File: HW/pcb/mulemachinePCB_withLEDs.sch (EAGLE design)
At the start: 31 parts, among them IC1 LD117AV50, IC2 MEGA8-P, J1 DCJ0202, Q1 16Mhz

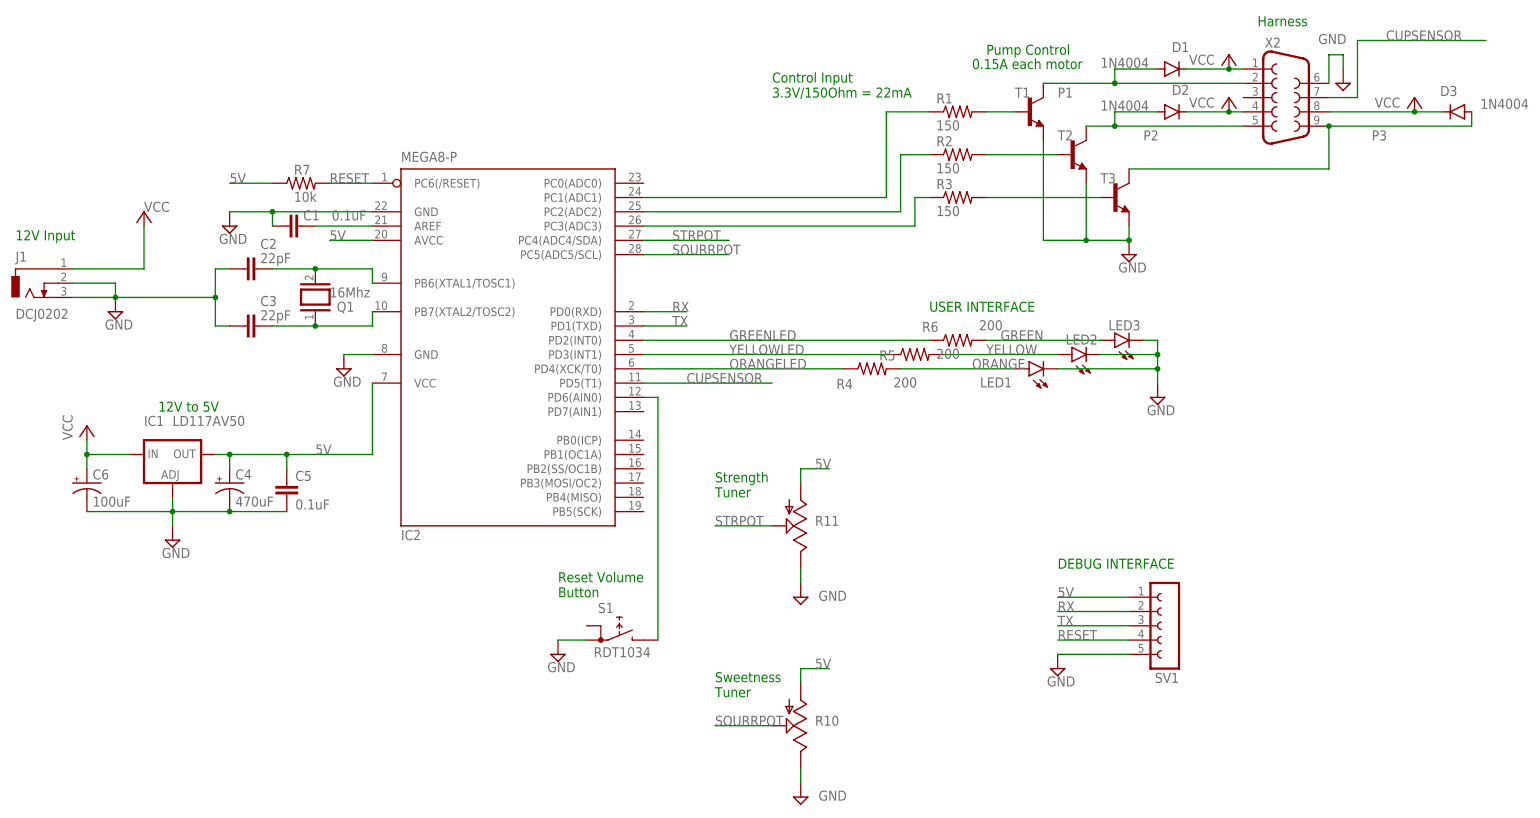
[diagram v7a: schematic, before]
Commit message: sourced push button and added to schematic and PCB layout. matched needed mounting to laser front panel cutout.
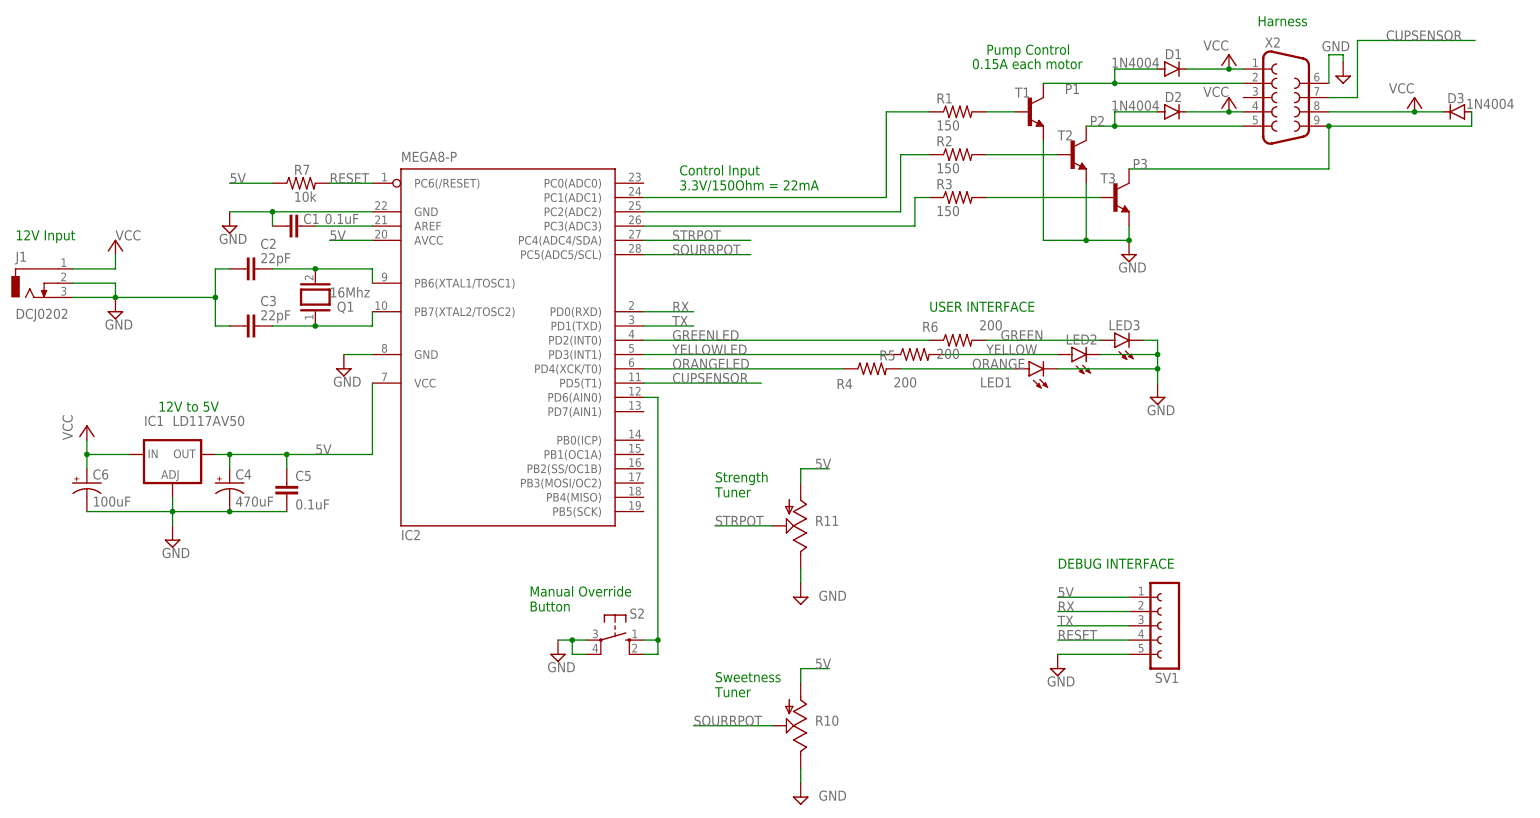
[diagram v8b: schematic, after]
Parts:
- removed S1: RDT1034, switch:RDT1034
- added S2: (no value), switch-omron:10-XX
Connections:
- net GND: now also S2.P, S2.P1; no longer S1.A1
- net N$24: now also S2.S, S2.S1; no longer S1.B
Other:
- note added: "Manual Override Button"
- note removed: "Reset Volume Button"
